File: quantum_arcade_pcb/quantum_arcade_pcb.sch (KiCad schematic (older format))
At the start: 472 parts, among them J20 J20, Q10 2N3904, Q11 2N3904, Q12 2N3906, Q13 2N3904, Q14 2N3904, Q15 2N6044, Q16 2N6044, Q17 2N3904, Q7 2N3904, Q8 2N3906, Q9 2N3904, SW1 SW_DIP_x08, SW2 SW_DIP_x08, Y1 12.096MHz

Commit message: 25 components left to place
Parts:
- C12, C13, C29, C30, C32, C4: footprint (none) -> quantum_arcade_pcb:CapSmall
- C14, C2, C20, C3, C35, C39, C40, C41, R26, R27, R39, R41, R46, R55, R59, R62, R66, R71, R73, R75, R76, R84, R85, R86, R95, R96, R97: footprint (none) -> quantum_arcade_pcb:GenComp
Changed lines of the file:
@@
 F 0 "C20" H 29325 29950 50  0000 L CNN
 F 1 ".1uF" H 29300 29775 50  0000 L CNN
-F 2 "" H 29513 29700 50  0001 C CNN
+F 2 "quantum_arcade_pcb:GenComp" H 29513 29700 50  0001 C CNN
 F 3 "" H 29475 29850 50  0001 C CNN
 	1    29475 29850
@@
 F 0 "R55" V 28980 30275 50  0000 C CNN
 F 1 "820" V 28900 30275 50  0000 C CNN
-F 2 "" V 28830 30275 50  0001 C CNN
+F 2 "quantum_arcade_pcb:GenComp" V 28830 30275 50  0001 C CNN
 F 3 "" H 28900 30275 50  0001 C CNN
 	1    28900 30275
@@
 F 0 "C35" H 40600 29875 50  0000 L CNN
 F 1 ".1uF" H 40600 29675 50  0000 L CNN
-F 2 "" H 40613 29625 50  0001 C CNN
+F 2 "quantum_arcade_pcb:GenComp" H 40613 29625 50  0001 C CNN
 F 3 "" H 40575 29775 50  0001 C CNN
 	1    40575 29775
@@
 F 0 "R59" V 34825 28625 50  0000 C CNN
 F 1 "470" V 34900 28625 50  0000 C CNN
-F 2 "" V 34830 28625 50  0001 C CNN
+F 2 "quantum_arcade_pcb:GenComp" V 34830 28625 50  0001 C CNN
 F 3 "" H 34900 28625 50  0001 C CNN
 	1    34900 28625
@@
 F 0 "R62" V 34225 29575 50  0000 C CNN
 F 1 "470" V 34300 29775 50  0000 C CNN
-F 2 "" V 34230 29775 50  0001 C CNN
+F 2 "quantum_arcade_pcb:GenComp" V 34230 29775 50  0001 C CNN
 F 3 "" H 34300 29775 50  0001 C CNN
 	1    34300 29775
@@
 F 0 "R66" V 35350 29275 50  0000 C CNN
 F 1 "3.9k" V 35425 29275 50  0000 C CNN
-F 2 "" V 35355 29275 50  0001 C CNN
+F 2 "quantum_arcade_pcb:GenComp" V 35355 29275 50  0001 C CNN
 F 3 "" H 35425 29275 50  0001 C CNN
 	1    35425 29275
@@
 F 0 "R76" V 35400 30825 50  0000 C CNN
 F 1 "1.2k" V 35475 30825 50  0000 C CNN
-F 2 "" V 35405 30825 50  0001 C CNN
+F 2 "quantum_arcade_pcb:GenComp" V 35405 30825 50  0001 C CNN
 F 3 "" H 35475 30825 50  0001 C CNN
 	1    35475 30825
@@
 F 0 "R75" V 35400 30600 50  0000 C CNN
 F 1 "100k" V 35475 30600 50  0000 C CNN
-F 2 "" V 35405 30600 50  0001 C CNN
+F 2 "quantum_arcade_pcb:GenComp" V 35405 30600 50  0001 C CNN
 F 3 "" H 35475 30600 50  0001 C CNN
 	1    35475 30600
@@
 F 0 "C32" V 35825 30675 50  0000 L CNN
 F 1 "100pf" V 35925 30675 50  0000 L CNN
-F 2 "" H 35913 30450 50  0001 C CNN
+F 2 "quantum_arcade_pcb:CapSmall" H 35913 30450 50  0001 C CNN
 F 3 "" H 35875 30600 50  0001 C CNN
 	1    35875 30600
@@
 F 0 "R71" V 36300 29300 50  0000 C CNN
 F 1 "5.6k" V 36375 29300 50  0000 C CNN
-F 2 "" V 36305 29300 50  0001 C CNN
+F 2 "quantum_arcade_pcb:GenComp" V 36305 29300 50  0001 C CNN
 F 3 "" H 36375 29300 50  0001 C CNN
 	1    36375 29300
@@
 F 0 "R73" V 37150 29575 50  0000 C CNN
 F 1 "10k" V 37225 29575 50  0000 C CNN
-F 2 "" V 37155 29575 50  0001 C CNN
+F 2 "quantum_arcade_pcb:GenComp" V 37155 29575 50  0001 C CNN
 F 3 "" H 37225 29575 50  0001 C CNN
 	1    37225 29575
@@
 F 0 "C29" V 37350 29900 50  0000 L CNN
 F 1 "39pf" V 37350 29700 50  0000 L CNN
-F 2 "" H 37263 29700 50  0001 C CNN
+F 2 "quantum_arcade_pcb:CapSmall" H 37263 29700 50  0001 C CNN
 F 3 "" H 37225 29850 50  0001 C CNN
 	1    37225 29850
@@
 F 0 "C30" V 37350 30250 50  0000 L CNN
 F 1 "100pf" V 37350 30000 50  0000 L CNN
-F 2 "" H 37263 30050 50  0001 C CNN
+F 2 "quantum_arcade_pcb:CapSmall" H 37263 30050 50  0001 C CNN
 F 3 "" H 37225 30200 50  0001 C CNN
 	1    37225 30200
@@
 F 0 "C3" H 14350 29975 50  0000 L CNN
 F 1 ".1uF" H 14325 29800 50  0000 L CNN
-F 2 "" H 14538 29725 50  0001 C CNN
+F 2 "quantum_arcade_pcb:GenComp" H 14538 29725 50  0001 C CNN
 F 3 "" H 14500 29875 50  0001 C CNN
 	1    14500 29875
@@
 F 0 "R26" V 14330 30050 50  0000 C CNN
 F 1 "820" V 14250 30050 50  0000 C CNN
-F 2 "" V 14180 30050 50  0001 C CNN
+F 2 "quantum_arcade_pcb:GenComp" V 14180 30050 50  0001 C CNN
 F 3 "" H 14250 30050 50  0001 C CNN
 	1    14250 30050
@@
 F 0 "C4" H 14075 30500 50  0000 L CNN
 F 1 ".01uF" H 14025 30325 50  0000 L CNN
-F 2 "" H 14288 30250 50  0001 C CNN
+F 2 "quantum_arcade_pcb:CapSmall" H 14288 30250 50  0001 C CNN
 F 3 "" H 14250 30400 50  0001 C CNN
 	1    14250 30400
@@
 F 0 "R27" V 14005 30300 50  0000 C CNN
 F 1 "820" V 13925 30300 50  0000 C CNN
-F 2 "" V 13855 30300 50  0001 C CNN
+F 2 "quantum_arcade_pcb:GenComp" V 13855 30300 50  0001 C CNN
 F 3 "" H 13925 30300 50  0001 C CNN
 	1    13925 30300
@@
 F 0 "C2" H 12975 29200 50  0000 L CNN
 F 1 ".1uF" H 12975 29000 50  0000 L CNN
-F 2 "" H 12988 28950 50  0001 C CNN
+F 2 "quantum_arcade_pcb:GenComp" H 12988 28950 50  0001 C CNN
 F 3 "" H 12950 29100 50  0001 C CNN
 	1    12950 29100
@@
 F 0 "R39" V 20375 29300 50  0000 C CNN
 F 1 "3.9k" V 20450 29300 50  0000 C CNN
-F 2 "" V 20380 29300 50  0001 C CNN
+F 2 "quantum_arcade_pcb:GenComp" V 20380 29300 50  0001 C CNN
 F 3 "" H 20450 29300 50  0001 C CNN
 	1    20450 29300
@@
 F 0 "C14" V 22325 28625 50  0000 L CNN
 F 1 ".1uF" V 22325 28450 50  0000 L CNN
-F 2 "" H 22488 28450 50  0001 C CNN
+F 2 "quantum_arcade_pcb:GenComp" H 22488 28450 50  0001 C CNN
 F 3 "" H 22450 28600 50  0001 C CNN
 	1    22450 28600
@@
 F 0 "R41" V 21325 29325 50  0000 C CNN
 F 1 "5.6k" V 21400 29325 50  0000 C CNN
-F 2 "" V 21330 29325 50  0001 C CNN
+F 2 "quantum_arcade_pcb:GenComp" V 21330 29325 50  0001 C CNN
 F 3 "" H 21400 29325 50  0001 C CNN
 	1    21400 29325
@@
 F 0 "R46" V 22175 29600 50  0000 C CNN
 F 1 "10k" V 22250 29600 50  0000 C CNN
-F 2 "" V 22180 29600 50  0001 C CNN
+F 2 "quantum_arcade_pcb:GenComp" V 22180 29600 50  0001 C CNN
 F 3 "" H 22250 29600 50  0001 C CNN
 	1    22250 29600
@@
 F 0 "C12" V 22375 29925 50  0000 L CNN
 F 1 "39pf" V 22375 29725 50  0000 L CNN
-F 2 "" H 22288 29725 50  0001 C CNN
+F 2 "quantum_arcade_pcb:CapSmall" H 22288 29725 50  0001 C CNN
 F 3 "" H 22250 29875 50  0001 C CNN
 	1    22250 29875
@@
 F 0 "C13" V 22375 30275 50  0000 L CNN
 F 1 "100pf" V 22375 30025 50  0000 L CNN
-F 2 "" H 22288 30075 50  0001 C CNN
+F 2 "quantum_arcade_pcb:CapSmall" H 22288 30075 50  0001 C CNN
 F 3 "" H 22250 30225 50  0001 C CNN
 	1    22250 30225
@@
 F 0 "C39" H 5325 30300 50  0000 L CNN
 F 1 ".1uF" H 5325 30100 50  0000 L CNN
-F 2 "" H 5338 30050 50  0001 C CNN
+F 2 "quantum_arcade_pcb:GenComp" H 5338 30050 50  0001 C CNN
 F 3 "" H 5300 30200 50  0001 C CNN
 	1    5300 30200
@@
 F 0 "C40" H 5325 31950 50  0000 L CNN
 F 1 ".1uF" H 5325 31750 50  0000 L CNN
-F 2 "" H 5338 31700 50  0001 C CNN
+F 2 "quantum_arcade_pcb:GenComp" H 5338 31700 50  0001 C CNN
 F 3 "" H 5300 31850 50  0001 C CNN
 	1    5300 31850
@@
 F 0 "C41" H 6525 31300 50  0000 L CNN
 F 1 ".01uF" H 6525 31100 50  0000 L CNN
-F 2 "" H 6538 31050 50  0001 C CNN
+F 2 "quantum_arcade_pcb:GenComp" H 6538 31050 50  0001 C CNN
 F 3 "" H 6500 31200 50  0001 C CNN
 	1    6500 31200
@@
 F 0 "R97" V 6630 31450 50  0000 C CNN
 F 1 "3.9K" V 6550 31450 50  0000 C CNN
-F 2 "" V 6480 31450 50  0001 C CNN
+F 2 "quantum_arcade_pcb:GenComp" V 6480 31450 50  0001 C CNN
 F 3 "" H 6550 31450 50  0001 C CNN
 	1    6550 31450
@@
 F 0 "R95" V 7355 30950 50  0000 C CNN
 F 1 "7.5K" V 7275 30950 50  0000 C CNN
-F 2 "" V 7205 30950 50  0001 C CNN
+F 2 "quantum_arcade_pcb:GenComp" V 7205 30950 50  0001 C CNN
 F 3 "" H 7275 30950 50  0001 C CNN
 	1    7275 30950
@@
 F 0 "R96" V 7355 31150 50  0000 C CNN
 F 1 "7.5K" V 7275 31150 50  0000 C CNN
-F 2 "" V 7205 31150 50  0001 C CNN
+F 2 "quantum_arcade_pcb:GenComp" V 7205 31150 50  0001 C CNN
 F 3 "" H 7275 31150 50  0001 C CNN
 	1    7275 31150
@@
 F 0 "R84" V 7630 29325 50  0000 C CNN
 F 1 "560" V 7550 29325 50  0000 C CNN
-F 2 "" V 7480 29325 50  0001 C CNN
+F 2 "quantum_arcade_pcb:GenComp" V 7480 29325 50  0001 C CNN
 F 3 "" H 7550 29325 50  0001 C CNN
 	1    7550 29325
@@
 F 0 "R85" V 8205 29050 50  0000 C CNN
 F 1 "7.5K" V 8125 29050 50  0000 C CNN
-F 2 "" V 8055 29050 50  0001 C CNN
+F 2 "quantum_arcade_pcb:GenComp" V 8055 29050 50  0001 C CNN
 F 3 "" H 8125 29050 50  0001 C CNN
 	1    8125 29050
@@
 F 0 "R86" V 8205 29250 50  0000 C CNN
 F 1 "7.5K" V 8125 29250 50  0000 C CNN
-F 2 "" V 8055 29250 50  0001 C CNN
+F 2 "quantum_arcade_pcb:GenComp" V 8055 29250 50  0001 C CNN
 F 3 "" H 8125 29250 50  0001 C CNN
 	1    8125 29250

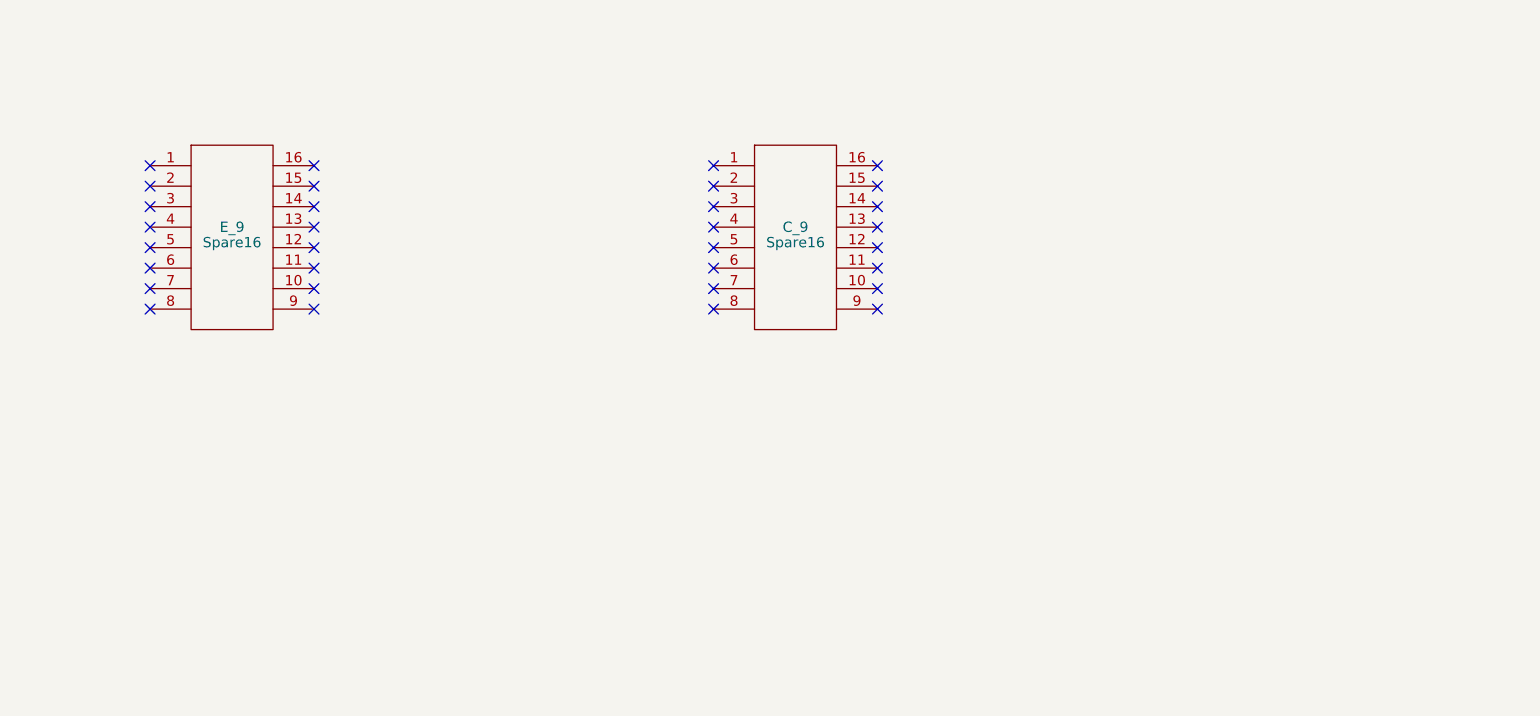
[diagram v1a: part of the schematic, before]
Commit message: Finished placing components
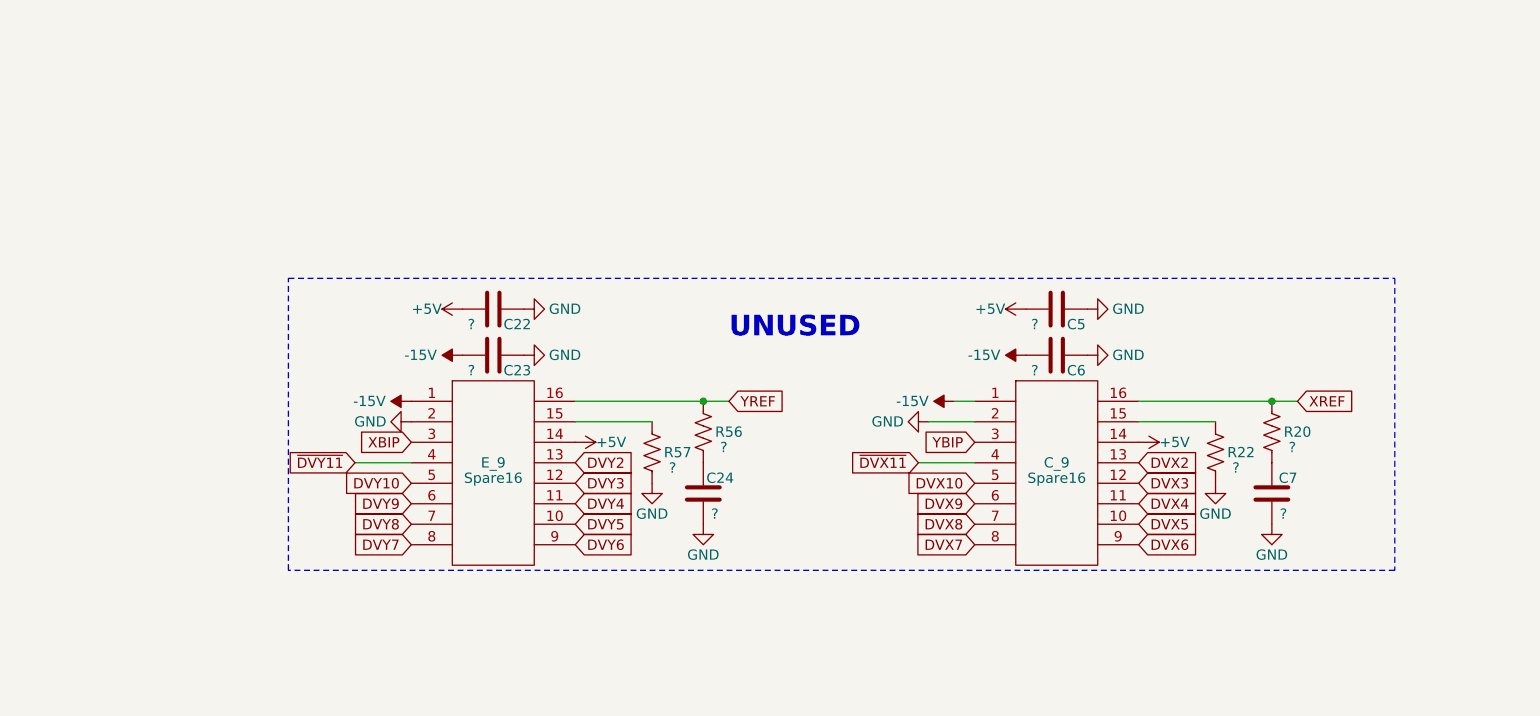
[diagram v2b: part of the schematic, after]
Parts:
- added C22, C23, C5, C6: ?, quantum_arcade_pcb:GenComp, symbol Device:C
- added C24, C7: ?, quantum_arcade_pcb:CapSmall, symbol Device:C
- added R20, R22, R56, R57: ?, quantum_arcade_pcb:GenComp, symbol Device:R_US
- C10, C17, C18, C26, C27, C36, C9, R106, R30, R31, R32, R33, R48, R49, R58, R90, R94: footprint (none) -> quantum_arcade_pcb:GenComp
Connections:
- net +5V: now also C_9.14, E_9.14, C22.2, C5.2
- net -15V: now also C_9.1, E_9.1, C23.2, C6.2
- net DVX10: now also C_9.5
- net DVX2: now also C_9.13
- net DVX3: now also C_9.12
- net DVX4: now also C_9.11
- net DVX5: now also C_9.10
- net DVX6: now also C_9.9
- net DVX7: now also C_9.8
- net DVX8: now also C_9.7
- net DVX9: now also C_9.6
- net DVY10: now also E_9.5
- net DVY2: now also E_9.13
- net DVY3: now also E_9.12
- net DVY4: now also E_9.11
- net DVY5: now also E_9.10
- net DVY6: now also E_9.9
- net DVY7: now also E_9.8
- net DVY8: now also E_9.7
- net DVY9: now also E_9.6
- net GND: now also C_9.2, E_9.2, C22.1, C23.1, C24.1, C5.1, C6.1, C7.1, R22.1, R57.1
- net XBIP: now also E_9.3
- net XREF: now also C_9.16, R20.2
- net YBIP: now also C_9.3
- net YREF: now also E_9.16, R56.2
- net ~DVX11: now also C_9.4
- net ~DVY11: now also E_9.4
- net at E_9.15: now also R57.2
- net at C_9.15: now also R22.2
- new net: C7.2, R20.1
- new net: C24.2, R56.1
- no-connect marks 144 -> 112
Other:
- note added: "UNUSED"
- moved on the sheet: C_9, E_9

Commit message: 1498 disconnected signals remain
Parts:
- J20: footprint Asteroids:J20 -> quantum_arcade_pcb:EdgeCon
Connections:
- net +5V: now also C71.2
- net GND: now also Y1.1; no longer C71.2, Y1.2
- net XBIP: now also C_9.3; no longer E_9.3
- net YBIP: now also E_9.3; no longer C_9.3
- net at C76.1, Q17.2 (B), R177.1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: now also Y1.2; no longer Y1.1
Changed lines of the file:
@@
 F 0 "J20" H 44625 29975 50  0000 C CNN
 F 1 "J20" H 44625 30125 50  0000 C CNN
-F 2 "Asteroids:J20" H 44525 30325 50  0001 C CNN
+F 2 "quantum_arcade_pcb:EdgeCon" H 44525 30325 50  0001 C CNN
 F 3 "" H 44525 30325 50  0001 C CNN
 	1    44625 30025
@@
 U 1 1 6AABD3DC
 P 1525 6025
-F 0 "Y1" V 1400 6075 50  0000 L CNN
-F 1 "12.096MHz" V 1650 6075 50  0000 L CNN
+F 0 "Y1" V 1375 5900 50  0000 L CNN
+F 1 "12.096MHz" V 1650 5575 50  0000 L CNN
 F 2 "quantum_arcade_pcb:Crystal" H 1525 6025 50  0001 C CNN
 F 3 "~" H 1525 6025 50  0001 C CNN
 	1    1525 6025
-	0    1    1    0
+	0    -1   -1   0
 $EndComp
 $Comp
@@
 Connection ~ 29550 20425
 $Comp
-L power:GND #PWR0377
-U 1 1 8230F494
-P 29550 20800
-F 0 "#PWR0377" H 29550 20550 50  0001 C CNN
-F 1 "GND" H 29550 20650 50  0000 C CNN
-F 2 "" H 29550 20800 50  0001 C CNN
-F 3 "" H 29550 20800 50  0001 C CNN
-	1    29550 20800
-	1    0    0    -1
-$EndComp
-$Comp
 L power:+5V #PWR0378
 U 1 1 8230FA57
@@
 $EndComp
 Text GLabel 43300 14375 0    50   Input ~ 0
-YBIP
-Text GLabel 40550 14375 0    50   Input ~ 0
 XBIP
+Text GLabel 40550 14375 0    50   Input ~ 0
+YBIP
 $Comp
 L power:-15V #PWR0556
@@
 Wire Notes Line
 	39950 15000 39950 13575
+$Comp
+L power:+5V #PWR0377
+U 1 1 617E0660
+P 29550 20800
+F 0 "#PWR0377" H 29550 20650 50  0001 C CNN
+F 1 "+5V" H 29675 20875 50  0000 C CNN
+F 2 "" H 29550 20800 50  0001 C CNN
+F 3 "" H 29550 20800 50  0001 C CNN
+	1    29550 20800
+	-1   0    0    1
+$EndComp
 $EndSCHEMATC

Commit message: Added more signal traces
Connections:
- net -15V: now also VR2.3 (VO); no longer VR2.2 (VI)
- net -24V: now also VR2.2 (VI); no longer VR2.3 (VO)
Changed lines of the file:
@@
 F 3 "" H 2675 1800 50  0001 C CNN
 	1    2675 1800
-	-1   0    0    1
+	1    0    0    1
 $EndComp
 $Comp
@@
 	0    1    1    0
 $EndComp
-$Comp
-L power:PWR_FLAG #FLG0103
-U 1 1 7F8A24B9
-P 42525 31025
-F 0 "#FLG0103" H 42525 31100 50  0001 C CNN
-F 1 "PWR_FLAG" H 42525 31198 50  0000 C CNN
-F 2 "" H 42525 31025 50  0001 C CNN
-F 3 "~" H 42525 31025 50  0001 C CNN
-	1    42525 31025
-	1    0    0    -1
-$EndComp
-$Comp
-L power:-15V #PWR0534
-U 1 1 7F8A395B
-P 42525 31025
-F 0 "#PWR0534" H 42525 31125 50  0001 C CNN
-F 1 "-15V" H 42540 31198 50  0000 C CNN
-F 2 "" H 42525 31025 50  0001 C CNN
-F 3 "" H 42525 31025 50  0001 C CNN
-	1    42525 31025
-	-1   0    0    1
-$EndComp
 Text GLabel 44850 20600 3    50   Input ~ 0
 ~MDTACK
@@
 	-1   0    0    1
 $EndComp
+$Comp
+L power:-24V #PWR0534
+U 1 1 62308FA3
+P 42550 31050
+F 0 "#PWR0534" H 42550 31150 50  0001 C CNN
+F 1 "-24V" H 42475 31200 50  0000 L CNN
+F 2 "" H 42550 31050 50  0001 C CNN
+F 3 "" H 42550 31050 50  0001 C CNN
+	1    42550 31050
+	-1   0    0    1
+$EndComp
+$Comp
+L power:PWR_FLAG #FLG0103
+U 1 1 6230A47A
+P 42550 31050
+F 0 "#FLG0103" H 42550 31125 50  0001 C CNN
+F 1 "PWR_FLAG" H 42550 31223 50  0000 C CNN
+F 2 "" H 42550 31050 50  0001 C CNN
+F 3 "~" H 42550 31050 50  0001 C CNN
+	1    42550 31050
+	1    0    0    -1
+$EndComp
 $EndSCHEMATC
